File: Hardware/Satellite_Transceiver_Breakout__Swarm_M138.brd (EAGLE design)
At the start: 35.6 x 88.9 mm, 97 parts, among them Q2 20V/4.2A/52mΩ/1.4W, Q4 20V/4.2A/52mΩ/1.4W, U1 CH340E_MSOP10, U2 SWARM_M138_TRANSCEIVER_MAIN, U3 3.3V

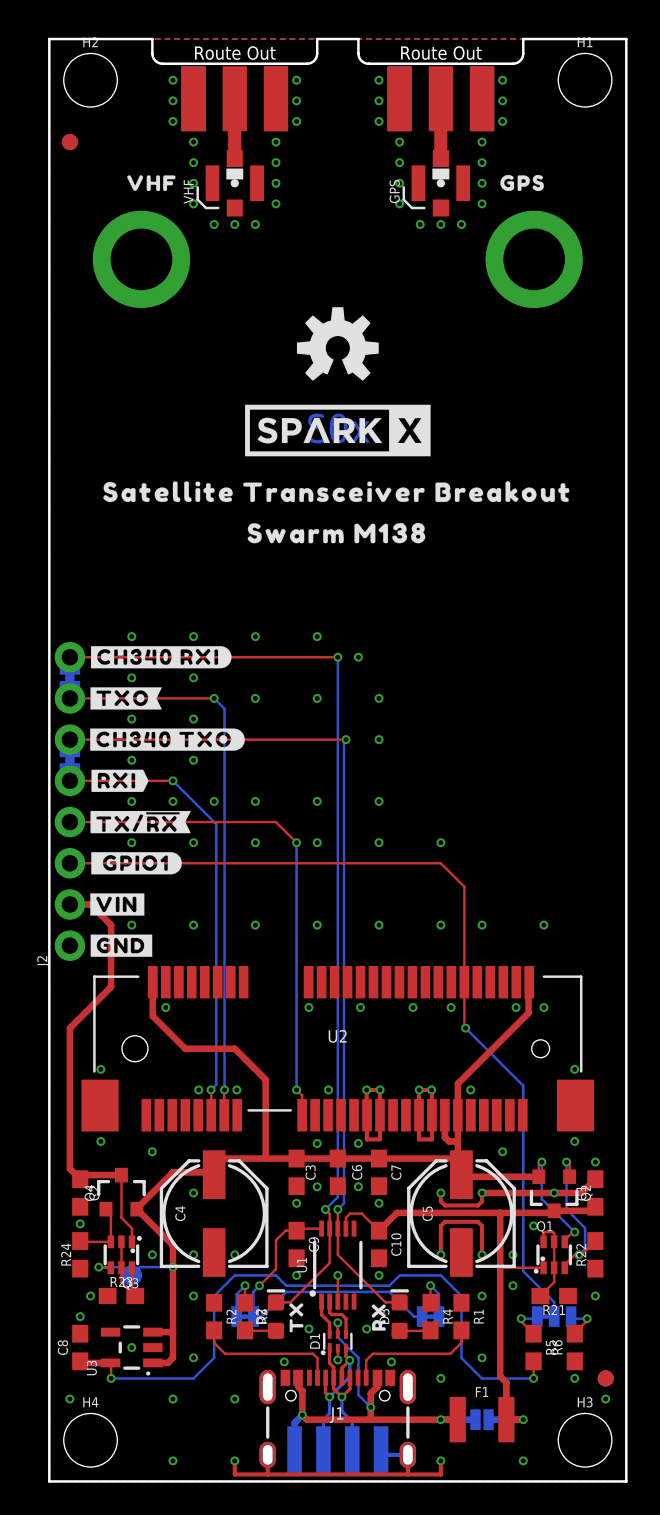
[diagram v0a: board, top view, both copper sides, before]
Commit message: Adds more measures, adds shield jumper, reduces polygon isolate to .007
* Adds new net class for RF traces between u.FL and SMA connectors to keep .01 isolate on those
particular traces
* Removes Sparkx silk and adds SparkFun silk
* Adds "Revised by" text
* Center aligns all schematic text
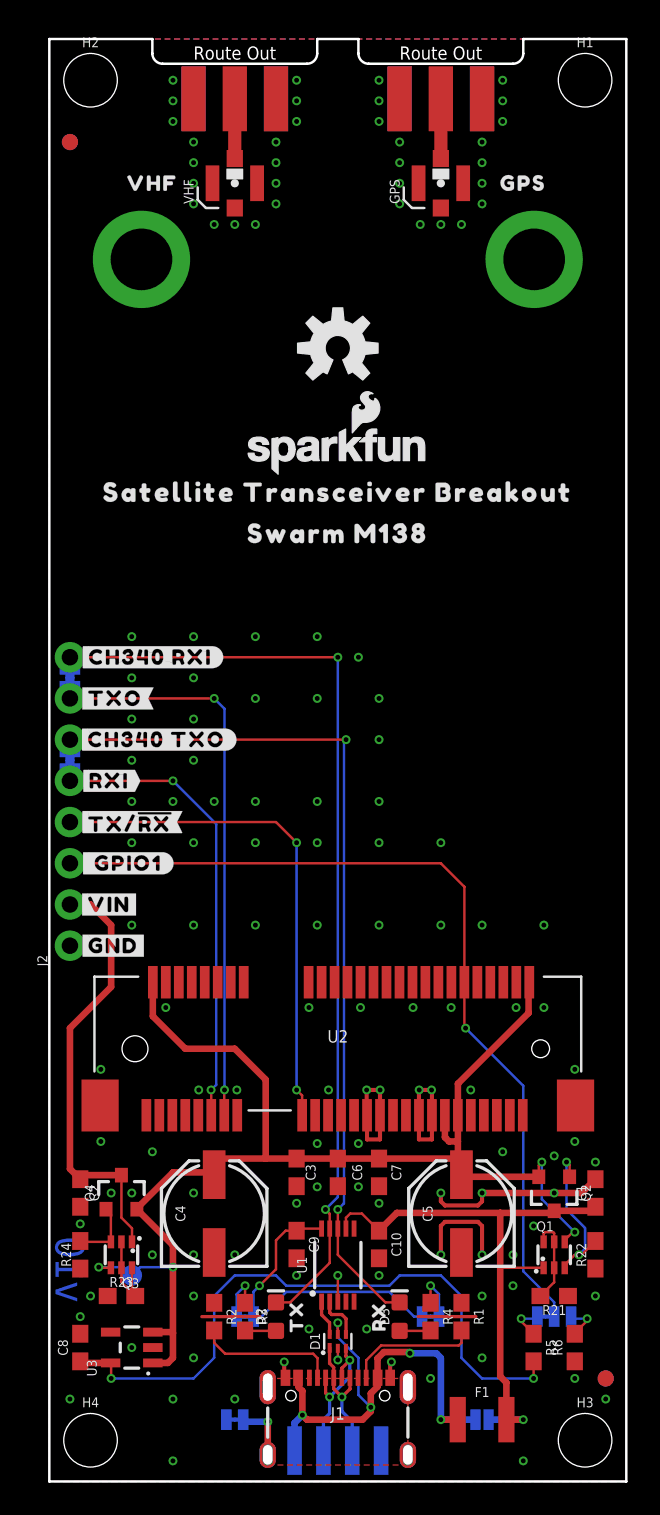
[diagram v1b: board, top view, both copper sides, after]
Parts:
- removed U$2: SPARKX-LOGO5, SparkX:SPARKX-LARGE
- added LOGO4: SFE_LOGO_NAME_FLAME.1_INCH, SparkFun-Aesthetics:SFE_LOGO_NAME_FLAME_.1
- added SHLD: JUMPER-SMT_2_NC_TRACE_SILK, SparkFun-Jumpers:SMT-JUMPER_2_NC_TRACE_SILK
- LOGO3: value OSHW-LOGOM -> SFE_LOGO_NAME_FLAME.1_INCH; device SparkFun-Aesthetics:OSHW-LOGO-M -> SparkFun-Aesthetics:SFE_LOGO_NAME_FLAME_.1
- U$1: value SPARKX-LOGO5 -> (none); device SparkX:SPARKX-LARGE -> top:#SHLD#14
- moved U$1 71.8 mm to (8.00, 3.81)
- moved LOGO3 7.62 mm to (17.8, 72.4)
- moved U$31 2.54 mm to (17.8, 59.7)
- moved U$32 2.54 mm to (17.8, 57.1)
- moved U$5 2.54 mm to (17.8, 64.8)
- moved U$6 2.54 mm to (17.8, 62.2)
- moved U$23 0.51 mm to (3.94, 33.0)
- moved U$24 0.51 mm to (3.94, 33.0)
- moved U$10 0.51 mm to (4.06, 48.3)
- moved U$11 0.51 mm to (6.60, 45.7)
- moved U$12 0.51 mm to (6.60, 45.7)
- moved U$13 0.51 mm to (3.68, 43.2)
- moved U$14 0.51 mm to (3.68, 43.2)
- moved U$15 0.51 mm to (4.95, 40.6)
- moved U$16 0.51 mm to (4.95, 40.6)
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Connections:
- new net SHLD: J1.SHLD1, J1.SHLD2, J1.SHLD3, J1.SHLD4, SHLD.2
- net GND: now also SHLD.1; no longer J1.SHLD1, J1.SHLD2, J1.SHLD3, J1.SHLD4
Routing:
- net GND: track 53.7 -> 44.3 mm, vias 136 -> 137
- net V_USB: track 26.1 -> 30.8 mm, vias 4 -> 5
- net SHLD: track 0.00 -> 3.69 mm, vias 0 -> 1
- added copper zone on layer 1, net SHLD
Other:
- board text added: "Revised By: Elias Santistevan"
- board text added: "v10"
- board text removed: "x03"
